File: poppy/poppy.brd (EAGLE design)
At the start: 100 x 80 mm, 5 parts, among them Q1 10MHz

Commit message: Refreshed to encoding
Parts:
- removed C5, C6: 22p, resistor:C1206K
- added C1, C2: 22p, resistor:C1206K
- added C3: 4u7, resistor:C1206K
- added ISP: ISP1, con-lstb:MA03-2
- Q1: device crystal:86SMX -> crystal:CTS406
- moved Q1 35.7 mm to (22.7, 44.1)
- moved U$1 17.8 mm to (6.39, 13.5), turned to 90 degrees
- moved EDGE 0.29 mm to (11.4, 0.00)
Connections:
- new net MISO: ISP.5, U$1.17
- new net MOSI: ISP.1, U$1.16
- new net N$4: C3.1, U$1.27
- new net RESET: ISP.3, U$1.24
- new net SCK: ISP.4, U$1.15
- net GND: now also C1.2, C2.2, C3.2, ISP.6; no longer C5.2, C6.2
- net N$1: now also C2.1, Q1.3; no longer C6.1, Q1.4
- net N$2: now also C1.1; no longer C5.1
- net VCC: now also ISP.2, U$1.31, U$1.32
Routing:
- net GND: track 103.1 -> 0.00 mm
- net VCC: track 32.2 -> 0.00 mm
- net N$1: track 13.1 -> 0.00 mm
- net N$2: track 8.10 -> 0.00 mm
- net D-: track 7.72 -> 0.00 mm
- net D+: track 7.51 -> 0.00 mm
- removed copper zone on layer 16, net N$3

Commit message: Routed
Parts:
- removed U$1: AT90USB162, at90usb:VQFP32
- added C4: 22p, resistor:C1206K
- added C5: 4u7, resistor:C1206K
- added C6: 100n, resistor:C1206K
- added LED1: LED, led:CHIPLED_0805
- added LED2: CON-RGB-LED-EXT, _led-rgb:CON-RGB-LED-TH-EXT
- added R1: 10k, resistor:R1206
- added R2: 1k, resistor:R1206
- added R3: 3k9, resistor:R1206
- added U1: ATUSB, at90usb:VQFP32
- added U2: MBI5039, _LedDrivers:SOP24-300-1.00
- C1: value 22p -> 100n; device resistor:C1206K -> resistor:C4532
- C2: value 22p -> 47u; device resistor:C1206K -> resistor:150CLZ-0810
- C3: value 4u7 -> 22p
- EDGE: value FULL-MINI-PCI-E -> (none)
- moved Q1 37.4 mm to (7.78, 9.86), turned to 90 degrees
- moved C2 28.5 mm to (24.6, 38.3), turned to 270 degrees
- moved C3 27.1 mm to (2.61, 9.30), turned to 90 degrees
- moved ISP 15.0 mm to (6.55, 24.4), flipped to the top, turned to 90 degrees
- moved C1 2.78 mm to (24.3, 28.8), turned to 180 degrees
- moved EDGE 0.34 mm to (11.1, -0.13)
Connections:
- removed net MOSI: ISP.1, U$1.16
- new net LATCH: U1.14, U2.4
- new net MOSI/DATA: ISP.1, U1.16, U2.2
- new net N$3: LED2.3.R, U2.5
- new net N$5: LED2.2.G, U2.6
- new net N$6: LED2.1.B, U2.7
- new net N$7: LED1.C, R2.2
- new net XTAL1: C3.1, Q1.1, U1.1
- new net XTAL2: C4.1, Q1.3, U1.2
- net D+: now also U1.29; no longer U$1.29
- net D-: now also U1.30; no longer U$1.30
- net GND: now also C2.-, C4.2, C5.2, C6.2, R2.1, R3.1, U1.28, U1.3, U2.1, U2.21; no longer C2.2, U$1.28, U$1.3
- net MISO: now also U1.17; no longer U$1.17
- net N$1: now also LED1.A, U1.25; no longer C2.1, Q1.3, U$1.2
- net N$2: now also R3.2, U2.23; no longer C1.1, Q1.1, U$1.1
- net N$4: now also C5.1, U1.27; no longer C3.1, U$1.27
- net RESET: now also R1.1, U1.24; no longer U$1.24
- net SCK: now also U1.15, U2.3; no longer U$1.15
- net VCC: now also C1.1, C2.+, C6.1, EDGE.2, LED2.4.VCC, R1.2, U1.31, U1.32, U1.4, U2.24; no longer EDGE.52, U$1.31, U$1.32, U$1.4
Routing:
- net GND: track 0.00 -> 72.2 mm
- net VCC: track 0.00 -> 47.7 mm
- net XTAL1: track 0.00 -> 19.9 mm
- net D-: track 0.00 -> 15.0 mm
- net D+: track 0.00 -> 14.9 mm
- net N$2: track 0.00 -> 9.01 mm
- net XTAL2: track 0.00 -> 7.32 mm
- net N$1: track 0.00 -> 5.08 mm
- net N$4: track 0.00 -> 4.65 mm
- net N$7: track 0.00 -> 2.68 mm

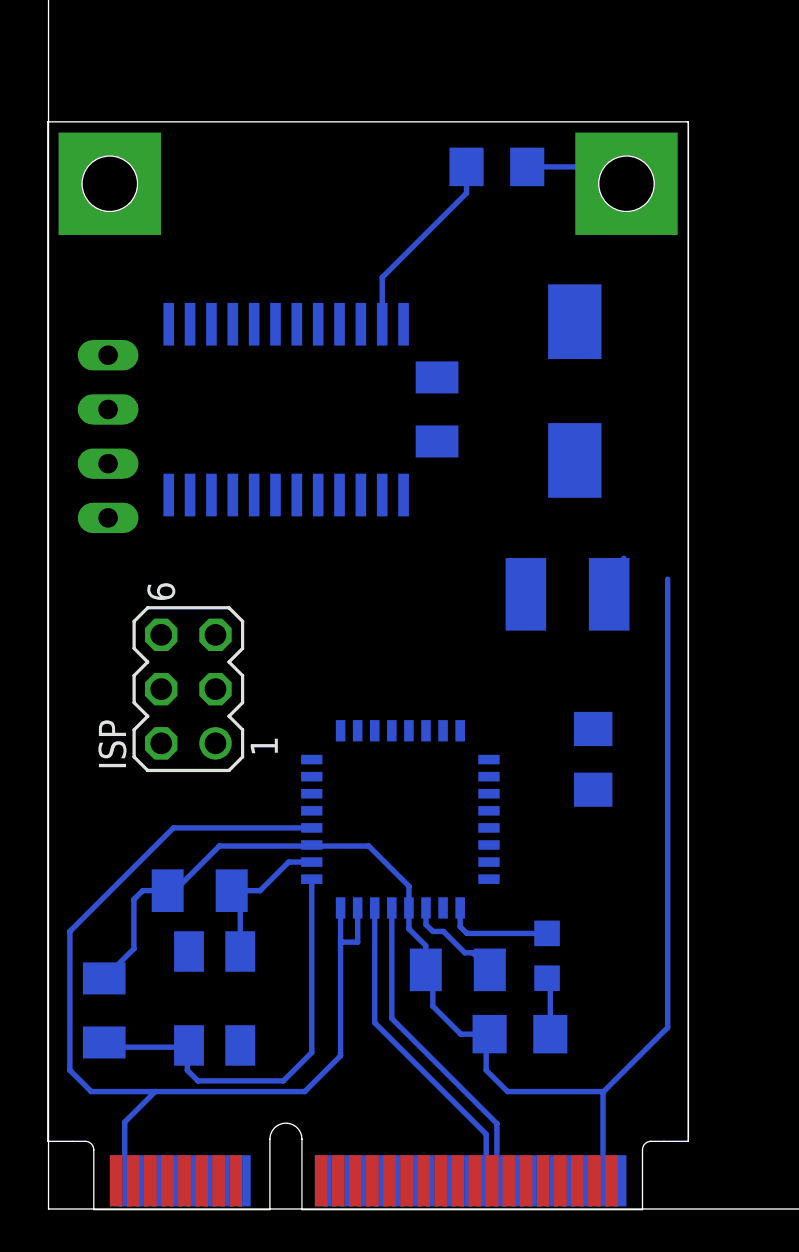
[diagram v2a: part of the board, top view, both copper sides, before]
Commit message: Routed 65%
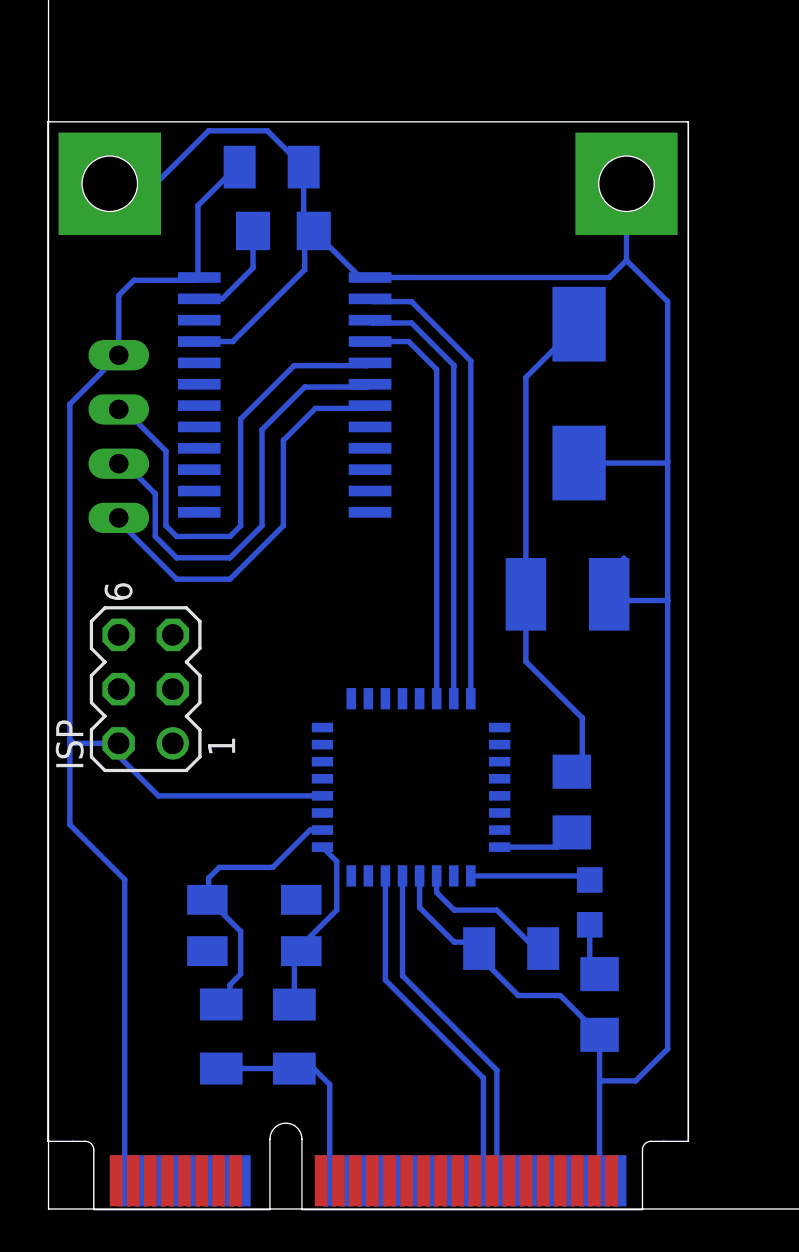
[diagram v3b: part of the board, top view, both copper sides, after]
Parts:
- moved C6 13.7 mm to (10.4, 48.8), turned to 180 degrees
- moved R3 10.4 mm to (11.0, 45.8)
- moved C3 8.99 mm to (11.5, 8.07), turned to 270 degrees
- moved C4 6.90 mm to (8.09, 8.08), turned to 270 degrees
- moved R2 3.98 mm to (25.8, 9.58), turned to 90 degrees
- moved Q1 3.89 mm to (9.64, 13.3), turned to 0 degrees
- moved LED1 3.20 mm to (25.4, 14.4)
- moved C5 2.69 mm to (21.7, 12.2)
- moved R1 2.24 mm to (24.5, 19.1)
- moved ISP 2.00 mm to (4.55, 24.4)
- moved U1 1.58 mm to (17.0, 19.8)
- moved U2 0.65 mm to (11.0, 38.1), turned to 270 degrees
- moved LED2 0.50 mm to (3.29, 36.2)
- moved C2 0.23 mm to (24.9, 38.2), turned to 90 degrees
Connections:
- new net GND18: C3.2, C4.2, EDGE.18
- net GND: no longer C3.2, C4.2
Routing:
- net VCC: track 47.7 -> 90.3 mm
- net GND: track 72.2 -> 112.9 mm
- net N$3: track 0.00 -> 22.6 mm
- net MOSI/DATA: track 0.00 -> 21.7 mm
- net N$5: track 0.00 -> 20.8 mm
- net SCK: track 0.00 -> 20.4 mm
- net LATCH: track 0.00 -> 19.1 mm
- net N$6: track 0.00 -> 18.8 mm
- net XTAL1: track 19.9 -> 8.47 mm
- net GND18: track 0.00 -> 9.90 mm
- net XTAL2: track 7.32 -> 13.3 mm
- net N$2: track 9.01 -> 4.85 mm
- net RESET: track 0.00 -> 3.66 mm
- net N$4: track 4.65 -> 6.86 mm
- net D+: track 14.9 -> 16.2 mm
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
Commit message: Ready to etch!
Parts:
- moved C2 27.4 mm to (24.1, 10.8), turned to 0 degrees
- moved ISP 24.1 mm to (25.2, 36.9), flipped to the bottom
- moved C4 16.2 mm to (5.84, 24.1)
- moved R2 14.3 mm to (26.1, 23.8)
- moved R3 13.8 mm to (24.6, 43.4)
- moved C3 12.2 mm to (9.07, 20.0), turned to 0 degrees
- moved Q1 12.1 mm to (9.78, 25.4), turned to 90 degrees
- moved C1 11.8 mm to (21.6, 17.3)
- moved R1 11.7 mm to (25.1, 30.7), turned to 180 degrees
- moved LED1 11.5 mm to (22.9, 25.6), turned to 90 degrees
- moved C5 10.5 mm to (20.7, 22.7)
- moved U1 10.5 mm to (17.5, 30.2)
- moved C6 5.65 mm to (16.1, 48.3)
- moved U2 5.36 mm to (15.2, 41.5), turned to 0 degrees
- moved LED2 2.06 mm to (3.79, 38.2)
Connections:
- removed net GND18: C3.2, C4.2, EDGE.18
- net GND: now also C3.2, C4.2
- net MISO: now also ISP.1; no longer ISP.5
- net MOSI/DATA: now also ISP.4; no longer ISP.1
- net RESET: now also ISP.5; no longer ISP.3
- net SCK: now also ISP.3; no longer ISP.4
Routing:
- net VCC: track 90.3 -> 156.1 mm
- net GND: track 112.9 -> 138.1 mm
- net D+: track 16.2 -> 31.9 mm
- net LATCH: track 19.1 -> 3.47 mm
- net D-: track 16.2 -> 31.8 mm
- net RESET: track 3.66 -> 18.9 mm
- net MOSI/DATA: track 21.7 -> 11.8 mm
- net GND18: track 9.90 -> 0.00 mm
- net SCK: track 20.4 -> 10.7 mm
- net N$3: track 22.6 -> 15.1 mm
- net N$5: track 20.8 -> 14.2 mm
- net N$6: track 18.8 -> 12.9 mm
- net XTAL1: track 8.47 -> 12.5 mm
- net XTAL2: track 13.3 -> 9.99 mm
- net MISO: track 0.00 -> 2.82 mm
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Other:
- board size 100 x 80 mm -> 39.8 x 57.2 mm
- board text added: "Poppy rev. 0 @meowthsli"
